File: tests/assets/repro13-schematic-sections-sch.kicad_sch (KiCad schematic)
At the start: 7 parts

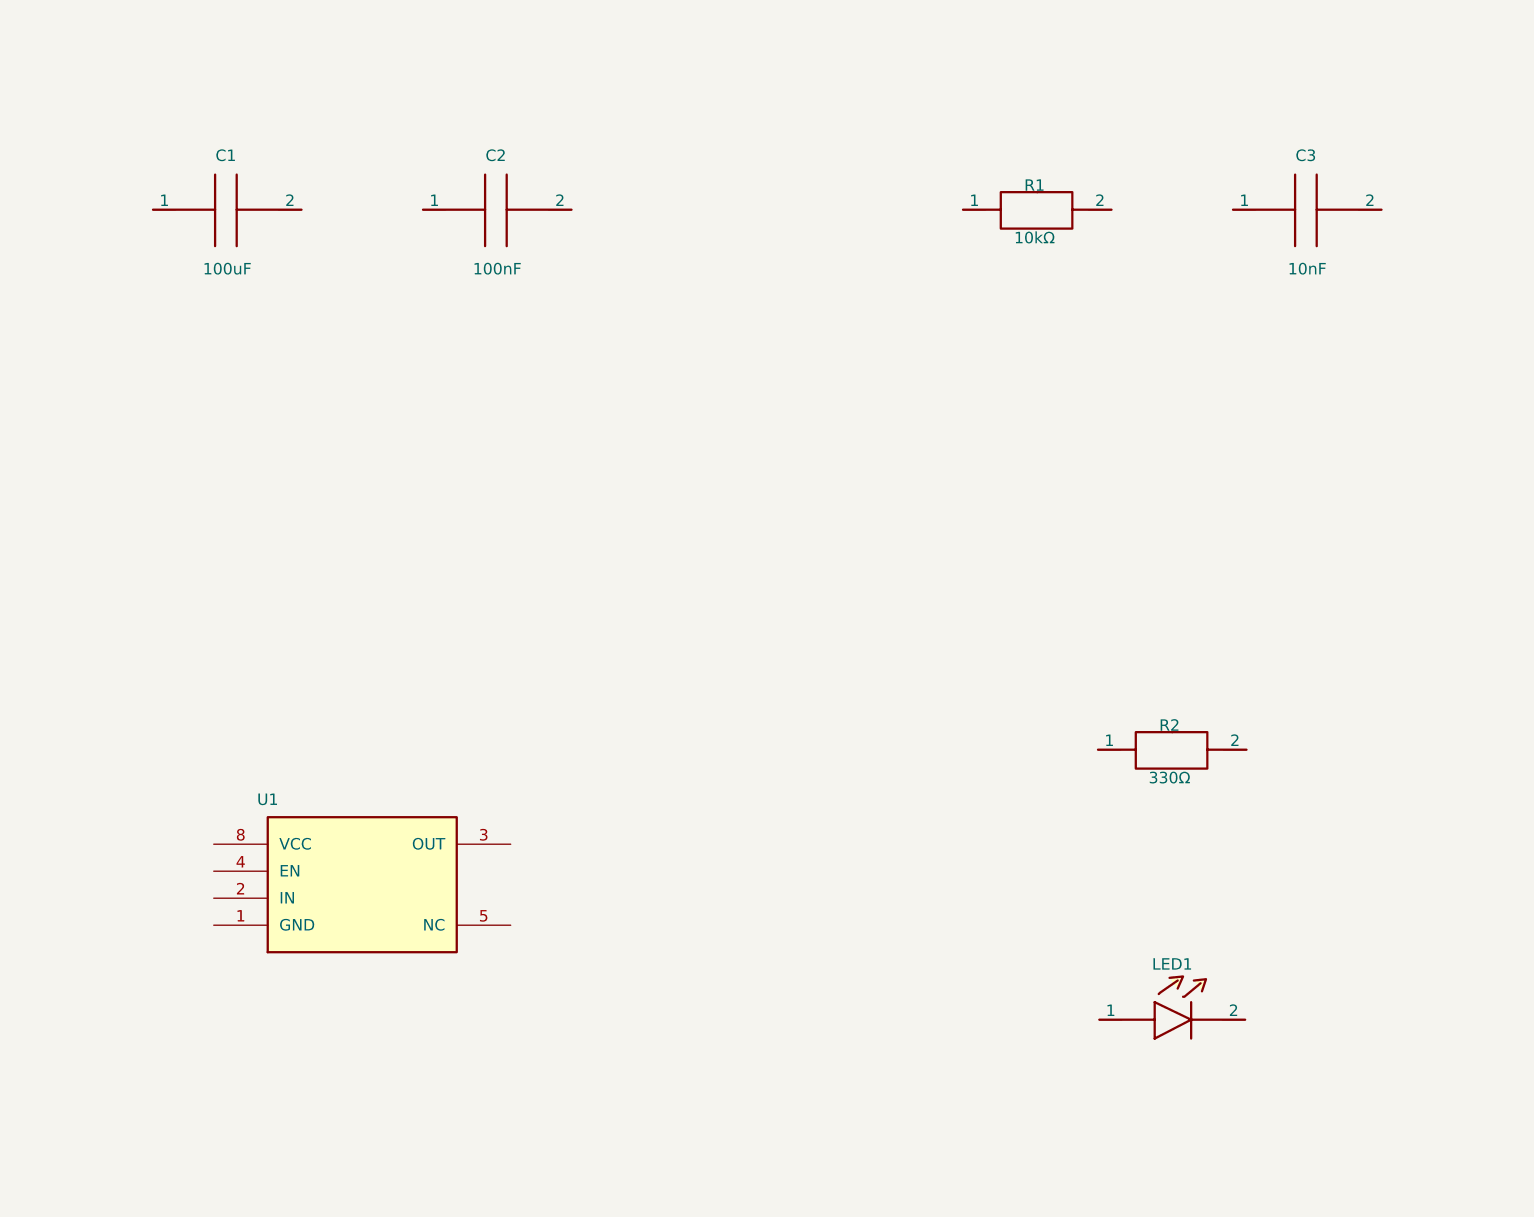
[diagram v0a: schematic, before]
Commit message: Render schematic sections as KiCad graphics in schematic export (#343)
* Render schematic sections conversion

* Use object color constants

* Fix review comments on schematic graphics stage

* Remove schematic section label offsets

* Rename schematic text offsets to padding

* Refresh schematic sections snapshot
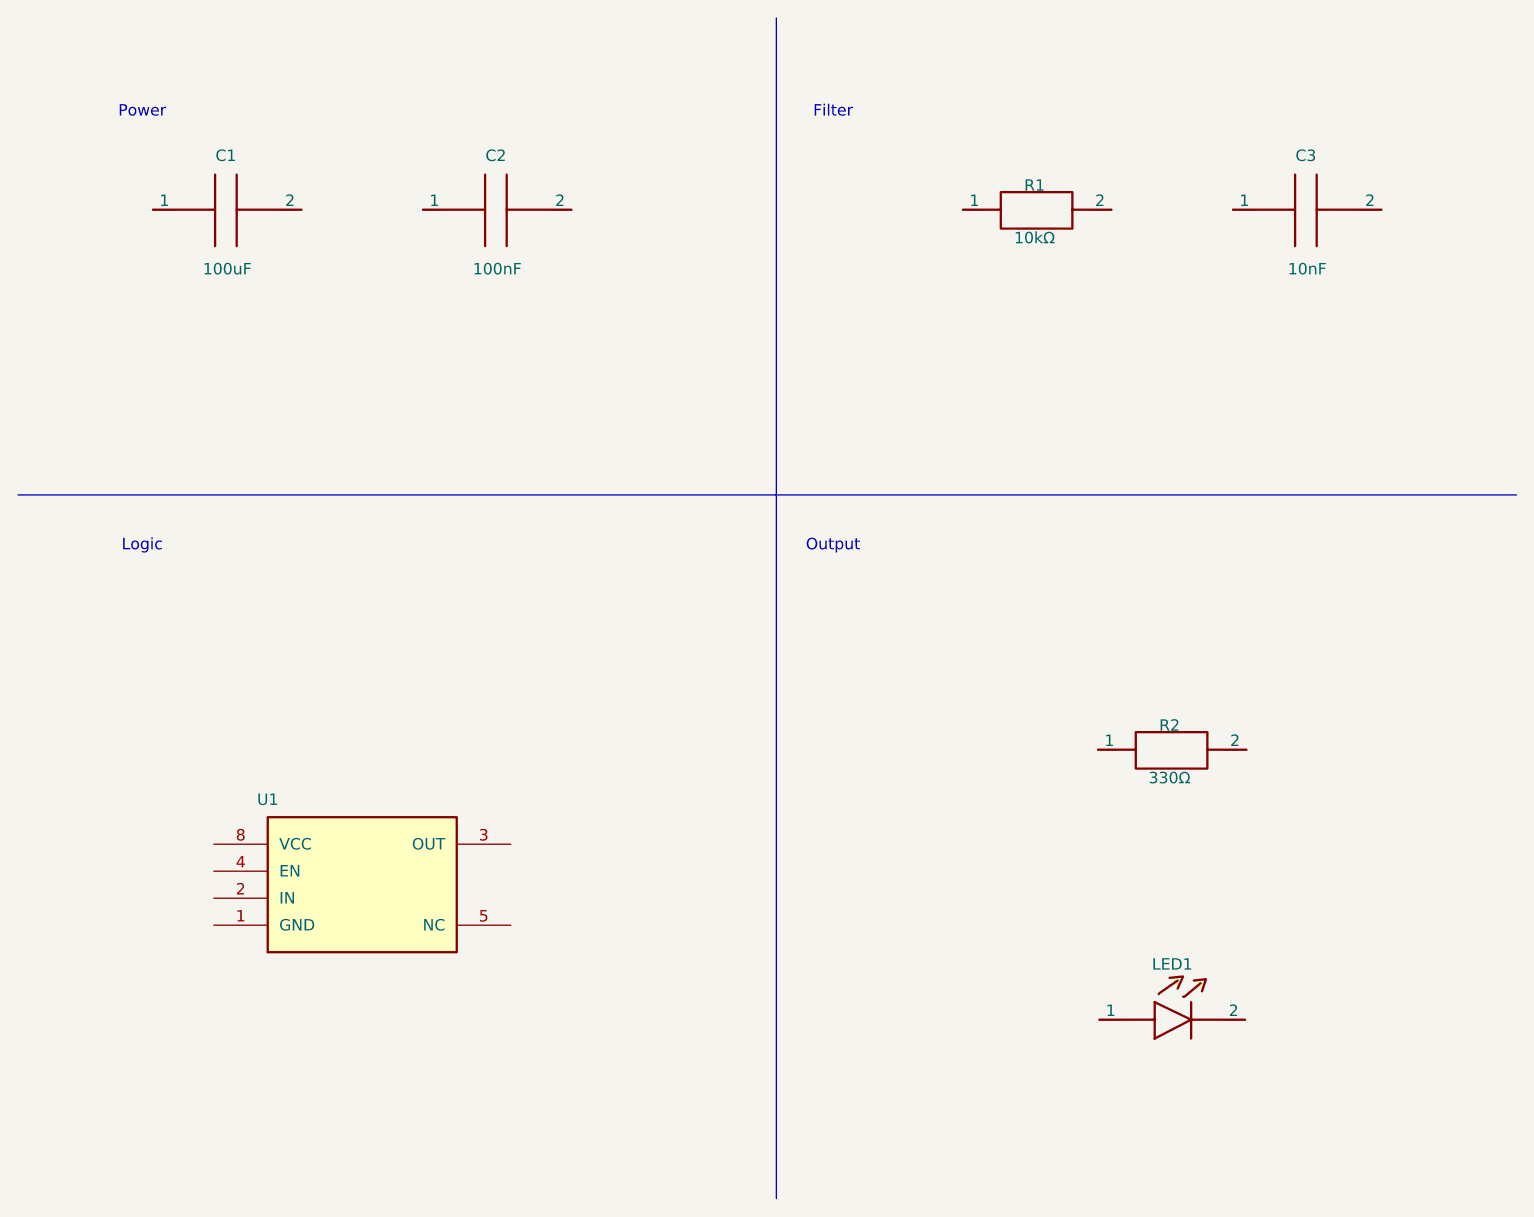
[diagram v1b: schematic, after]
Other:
- note added: "Filter"
- note added: "Logic"
- note added: "Output"
- note added: "Power"
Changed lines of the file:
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@@
     (instances
       (project ""
-        (path "/384f0f5b-5222-4538-8a53-443e61b77923"
+        (path "/be83095d-0909-4ad2-a7fa-ecf97d2a40e9"
           (reference "C1")
           (unit 1)
@@
     (instances
       (project ""
-        (path "/384f0f5b-5222-4538-8a53-443e61b77923"
+        (path "/be83095d-0909-4ad2-a7fa-ecf97d2a40e9"
           (reference "C2")
           (unit 1)
@@
     (instances
       (project ""
-        (path "/384f0f5b-5222-4538-8a53-443e61b77923"
+        (path "/be83095d-0909-4ad2-a7fa-ecf97d2a40e9"
           (reference "R1")
           (unit 1)
@@
     (instances
       (project ""
-        (path "/384f0f5b-5222-4538-8a53-443e61b77923"
+        (path "/be83095d-0909-4ad2-a7fa-ecf97d2a40e9"
           (reference "C3")
           (unit 1)
@@
     (instances
       (project ""
-        (path "/384f0f5b-5222-4538-8a53-443e61b77923"
+        (path "/be83095d-0909-4ad2-a7fa-ecf97d2a40e9"
           (reference "U1")
           (unit 1)
@@
     (instances
       (project ""
-        (path "/384f0f5b-5222-4538-8a53-443e61b77923"
+        (path "/be83095d-0909-4ad2-a7fa-ecf97d2a40e9"
           (reference "R2")
           (unit 1)
@@
     (instances
       (project ""
-        (path "/384f0f5b-5222-4538-8a53-443e61b77923"
+        (path "/be83095d-0909-4ad2-a7fa-ecf97d2a40e9"
           (reference "LED1")
           (unit 1)
@@
     )
   )
+  (text "Power"
+    (at 79.05 49.912499999999994 0)
+    (effects
+      (font
+        (size 1.27 1.27)
+        (color 0 0 0 1)
+      )
+    )
+  )
+  (text "Filter"
+    (at 155.8125 49.912499999999994 0)
+    (effects
+      (font
+        (size 1.27 1.27)
+        (color 0 0 0 1)
+      )
+    )
+  )
+  (text "Logic"
+    (at 79.05 98.104084875 0)
+    (effects
+      (font
+        (size 1.27 1.27)
+        (color 0 0 0 1)
+      )
+    )
+  )
+  (text "Output"
+    (at 155.8125 98.104084875 0)
+    (effects
+      (font
+        (size 1.27 1.27)
+        (color 0 0 0 1)
+      )
+    )
+  )
+  (polyline
+    (pts
+      (xy 65.25 92.404084875)
+      (xy 231.75 92.404084875)
+    )
+    (stroke
+      (width 0)
+      (type default)
+      (color 0 0 0 1)
+    )
+  )
+  (polyline
+    (pts
+      (xy 149.5125 170.58749999999998)
+      (xy 149.5125 39.41249999999998)
+    )
+    (stroke
+      (width 0)
+      (type default)
+      (color 0 0 0 1)
+    )
+  )
